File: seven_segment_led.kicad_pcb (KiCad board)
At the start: 2 copper layers, 80 x 62.2 mm, 11 parts, among them J1 Conn_01x05, U1 74HC595, U2 7SEGMENT_CA

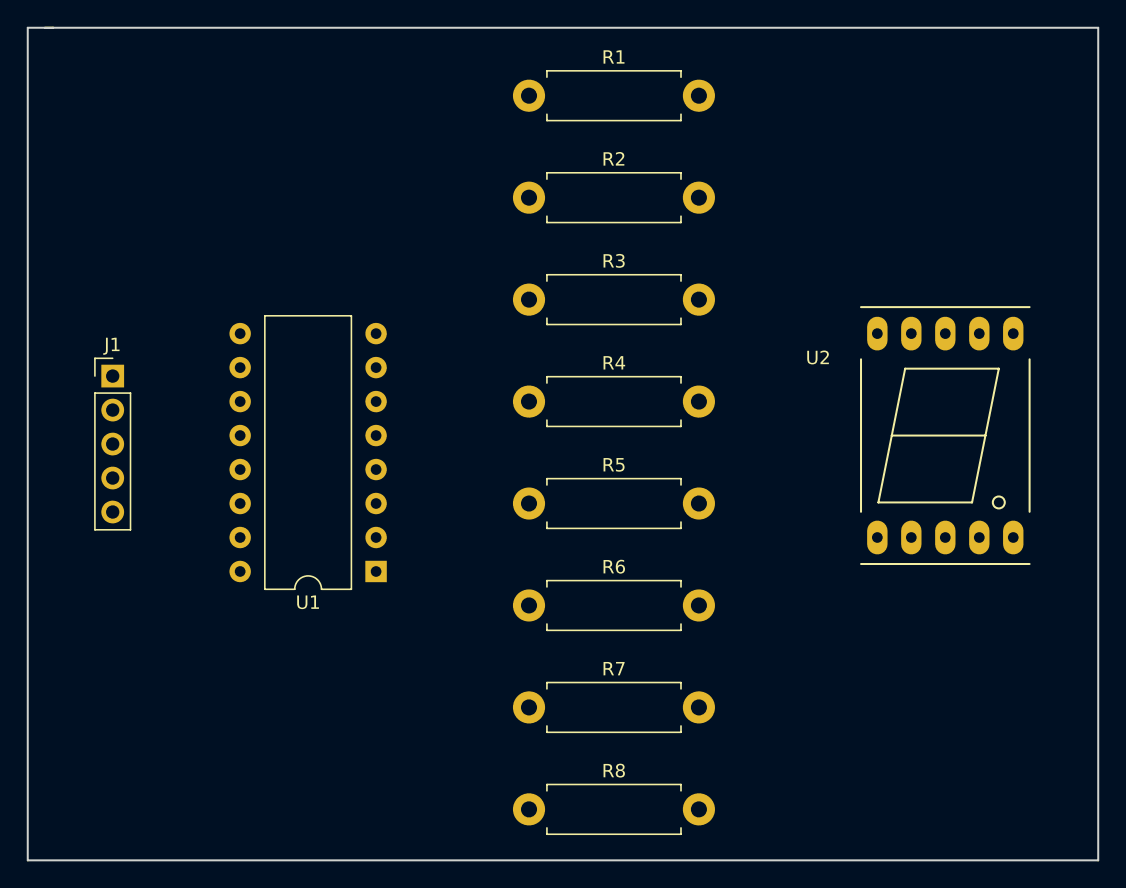
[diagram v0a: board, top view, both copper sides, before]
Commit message: Final layout. No gerbers will be produced
Signed-off-by: Richard Memory <richardfmemory@gmail.com>
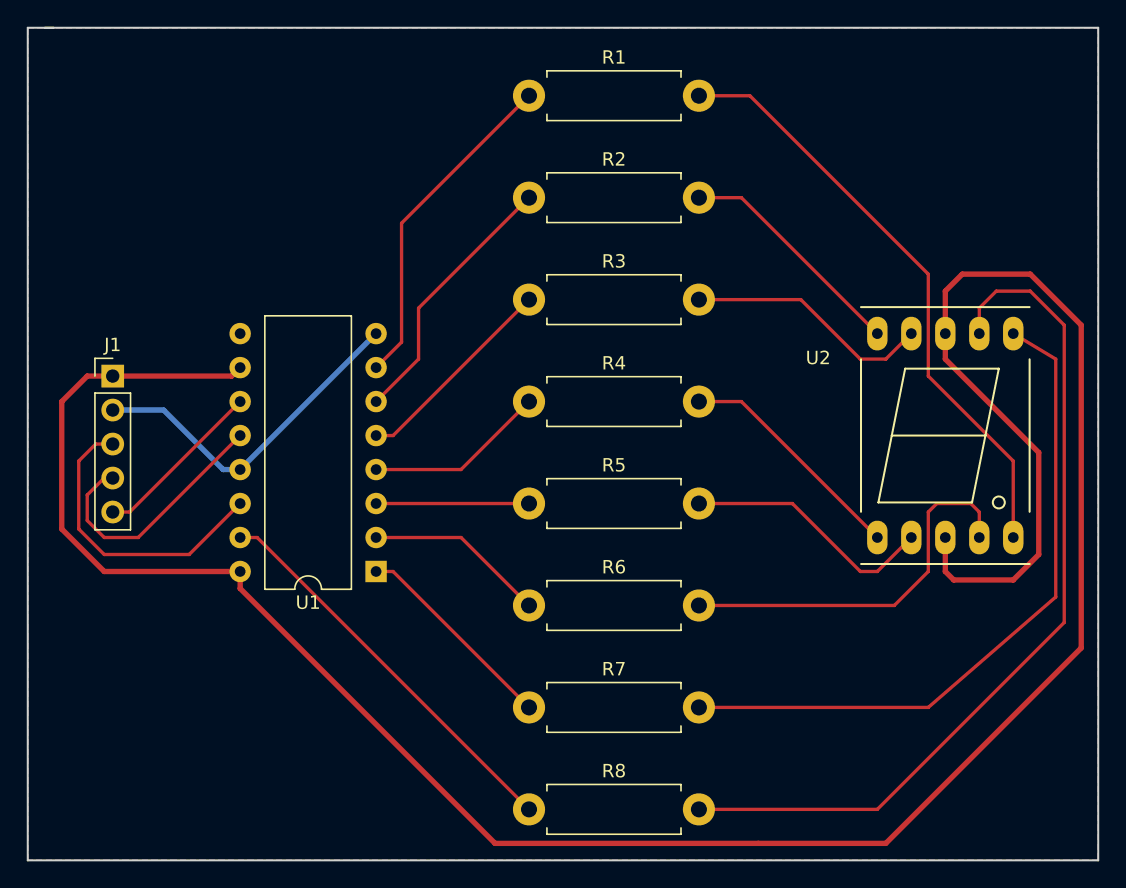
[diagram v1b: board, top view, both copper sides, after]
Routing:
- net VCC: track 0.00 -> 186.2 mm
- net Net-(R8-Pad2): track 0.00 -> 65.1 mm
- net Net-(R7-Pad2): track 0.00 -> 51.2 mm
- net Net-(R1-Pad2): track 0.00 -> 45.0 mm
- net /sg0: track 0.00 -> 30.0 mm
- net Net-(R6-Pad2): track 0.00 -> 28.9 mm
- net GND: track 0.00 -> 25.7 mm
- net /sg7: track 0.00 -> 25.1 mm
- net /LATCH: track 0.00 -> 22.6 mm
- net /sg6: track 0.00 -> 20.0 mm
- net /CLOCK: track 0.00 -> 19.4 mm
- net Net-(R5-Pad2): track 0.00 -> 19.0 mm
- net Net-(R3-Pad2): track 0.00 -> 18.5 mm
- net Net-(R2-Pad2): track 0.00 -> 17.5 mm
- net Net-(R4-Pad2): track 0.00 -> 17.5 mm
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- added copper zone on B.Cu, net GND
- added copper zone on F.Cu, net VCC
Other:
- net class Power added: clearance 0.3, trace_width 0.4, via_dia 0.7, via_drill 0.5
